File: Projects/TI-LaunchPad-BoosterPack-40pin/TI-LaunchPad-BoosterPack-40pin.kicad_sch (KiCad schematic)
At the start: 2 parts, among them J2-J4 Conn_01x10, J3-J1 Conn_01x10

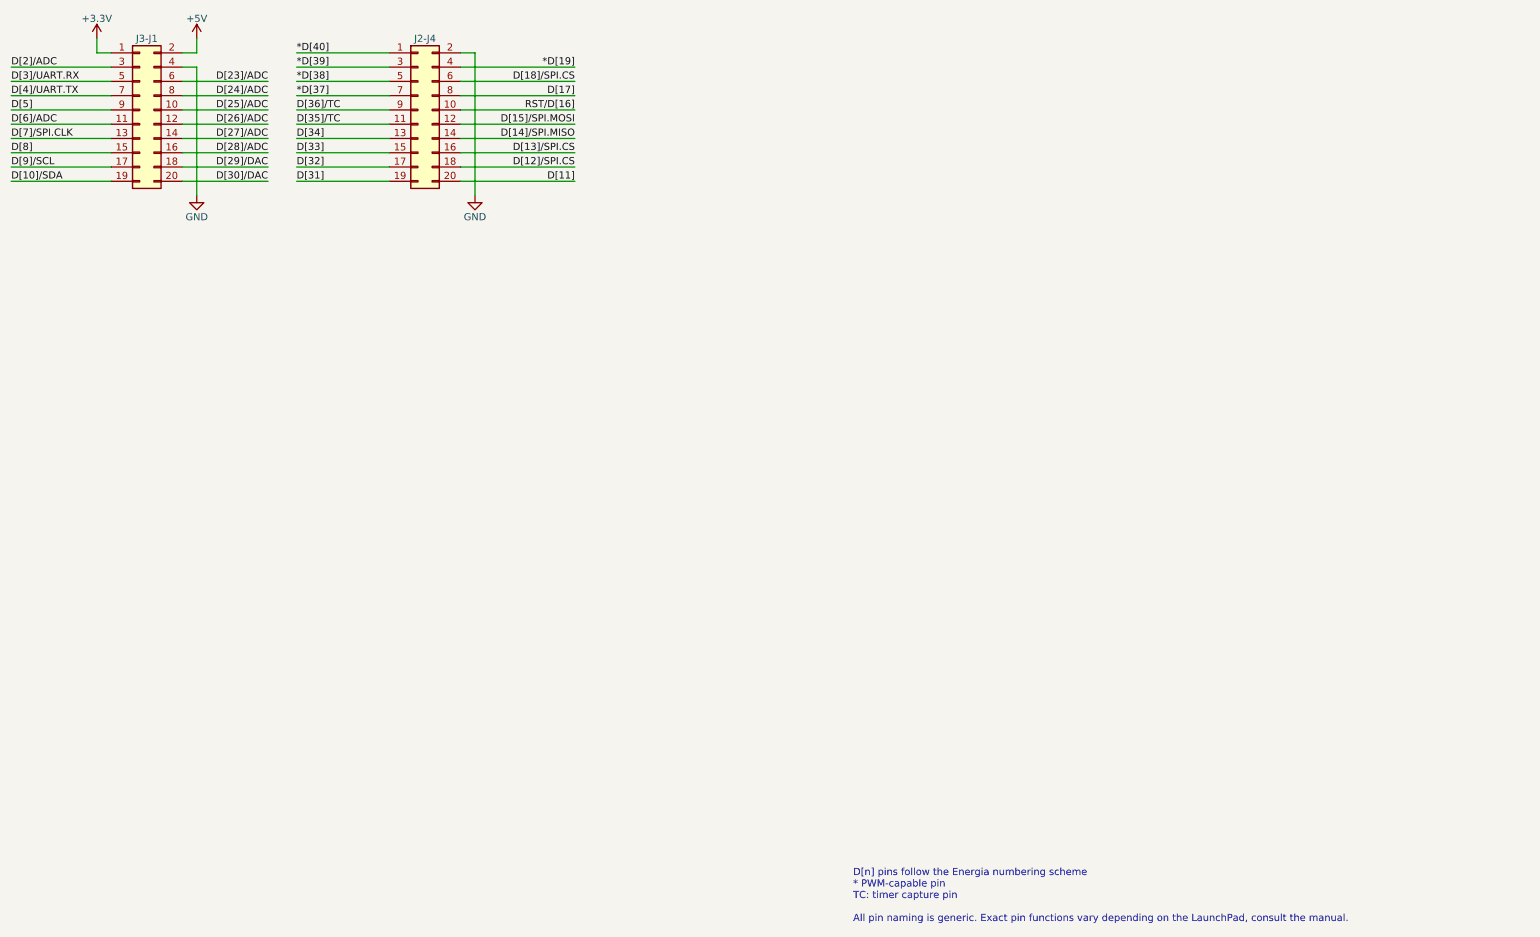
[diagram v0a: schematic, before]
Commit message: Update projects for KiCad version 7
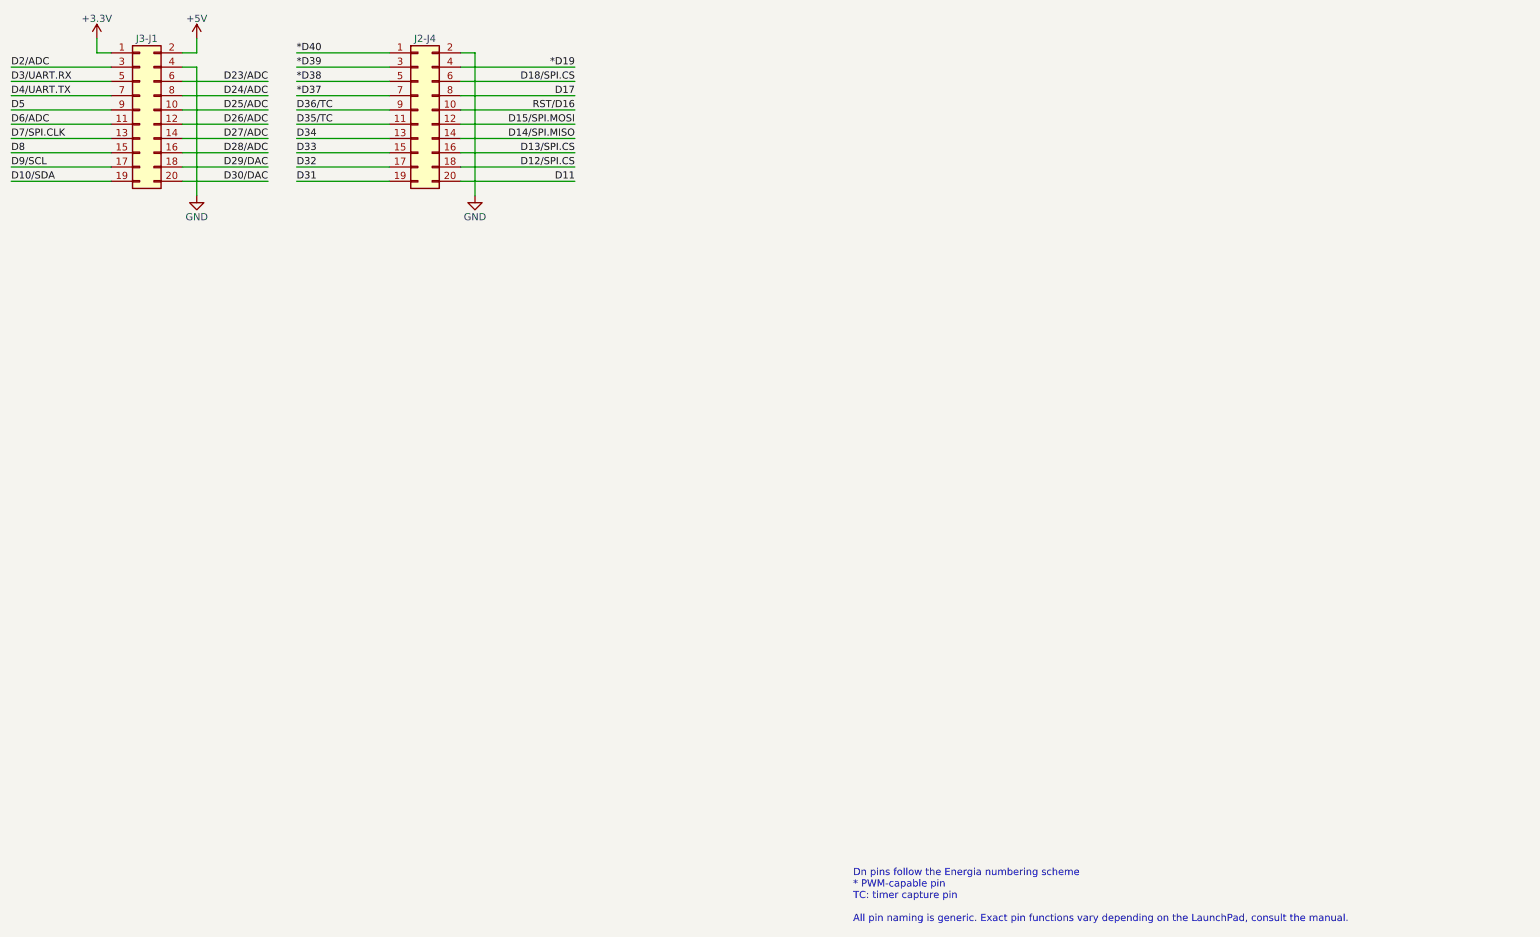
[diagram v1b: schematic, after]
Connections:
- net *D[19] renamed *D19
- net *D[37] renamed *D37
- net *D[38] renamed *D38
- net *D[39] renamed *D39
- net *D[40] renamed *D40
- net D[10]/SDA renamed D10/SDA
- net D[11] renamed D11
- net D[12]/SPI.CS renamed D12/SPI.CS
- net D[13]/SPI.CS renamed D13/SPI.CS
- net D[14]/SPI.MISO renamed D14/SPI.MISO
- net D[15]/SPI.MOSI renamed D15/SPI.MOSI
- net D[17] renamed D17
- net D[18]/SPI.CS renamed D18/SPI.CS
- net D[23]/ADC renamed D23/ADC
- net D[24]/ADC renamed D24/ADC
- net D[25]/ADC renamed D25/ADC
- net D[26]/ADC renamed D26/ADC
- net D[27]/ADC renamed D27/ADC
- net D[28]/ADC renamed D28/ADC
- net D[29]/DAC renamed D29/DAC
- net D[2]/ADC renamed D2/ADC
- net D[30]/DAC renamed D30/DAC
- net D[31] renamed D31
- net D[32] renamed D32
- net D[33] renamed D33
- net D[34] renamed D34
- net D[35]/TC renamed D35/TC
- net D[36]/TC renamed D36/TC
- net D[3]/UART.RX renamed D3/UART.RX
- net D[4]/UART.TX renamed D4/UART.TX
- net D[5] renamed D5
- net D[6]/ADC renamed D6/ADC
- net D[7]/SPI.CLK renamed D7/SPI.CLK
- net D[8] renamed D8
- net D[9]/SCL renamed D9/SCL
- net RST/D[16] renamed RST/D16
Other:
- note added: "Dn pins follow the Energia numbering scheme * PWM-capable pin TC: timer capture pin All pin naming is generic. Exact pin functions vary depending on the LaunchPad, consult the manual."
- note removed: "D[n] pins follow the Energia numbering scheme * PWM-capable pin TC: timer capture pin All pin naming is generic. Exact pin functions vary depending on the LaunchPad, consult the manual."

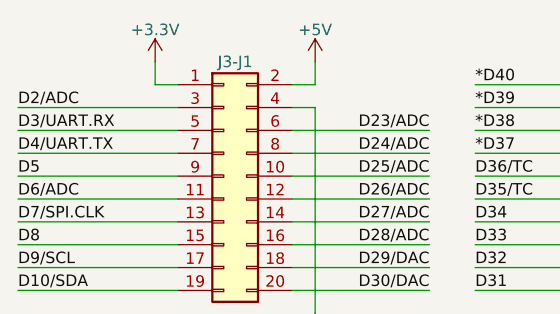
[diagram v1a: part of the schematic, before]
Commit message: Update templates to V8 format
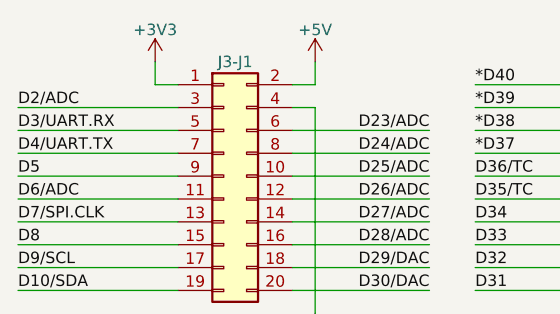
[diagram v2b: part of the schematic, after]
